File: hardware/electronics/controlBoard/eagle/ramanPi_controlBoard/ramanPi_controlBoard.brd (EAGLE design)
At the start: 149.8 x 98.7 mm, 17 parts

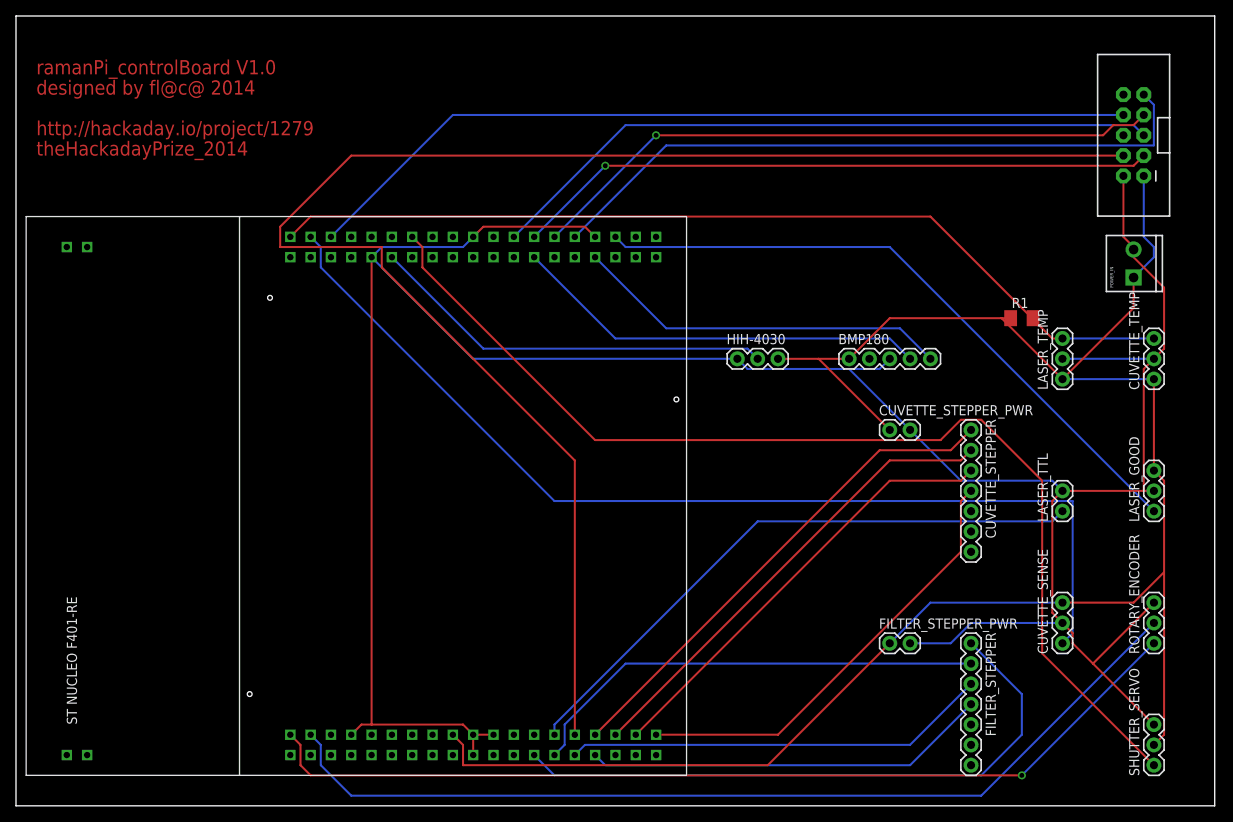
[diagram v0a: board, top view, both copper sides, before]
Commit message: re-routed controlBoard layout
controlBoard board layout redone..
Adjusted stepper controller placement
Adjusted board size
Added svg exports for top and bottom layers
Added top and bottom studio files for cameo
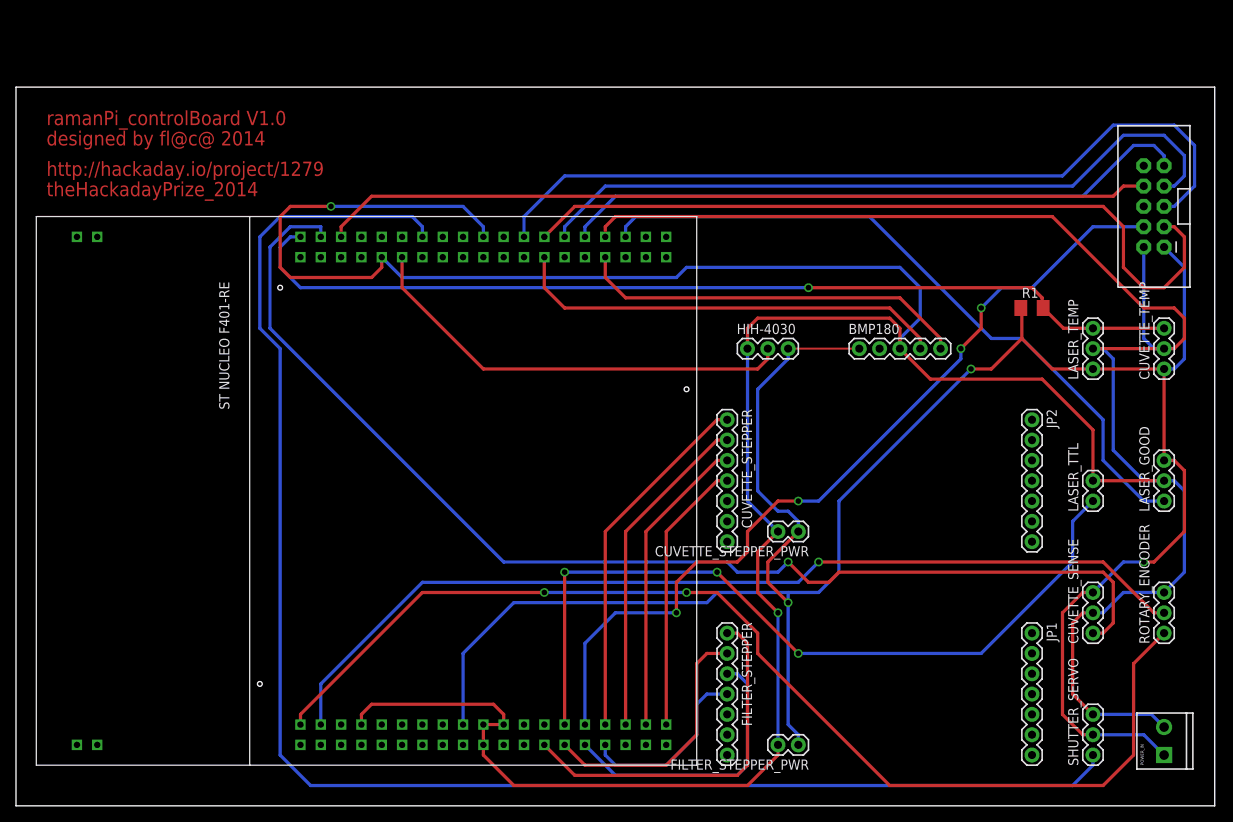
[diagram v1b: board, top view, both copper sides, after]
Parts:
- added JP1, JP2: (no value), SparkFun-Connectors:1X07
- moved POWER_IN 59.8 mm to (143.5, 6.35)
- moved CUVETTE_STEPPER 30.5 mm to (88.9, 48.3)
- moved FILTER_STEPPER 30.5 mm to (88.9, 21.6)
- moved CUVETTE_STEPPER_PWR 17.1 mm to (97.8, 34.3), turned to 180 degrees
- moved FILTER_STEPPER_PWR 17.1 mm to (97.8, 7.62), turned to 180 degrees
- moved POWER_CONTROL_BOARD 9.25 mm to (142.2, 74.9)
- moved SHUTTER_SERVO 7.73 mm to (134.6, 6.35)
- moved LASER_TTL 4.02 mm to (134.6, 38.1)
- moved CUVETTE_SENSE 4.02 mm to (134.6, 21.6)
- moved LASER_TEMP 4.02 mm to (134.6, 54.6)
- moved U$1 1.80 mm to (85.1, 5.08)
- moved BMP180 1.80 mm to (105.4, 57.1)
- moved HIH-4030 1.80 mm to (91.4, 57.1)
- moved R1 1.80 mm to (127.0, 62.2)
- moved LASER_GOOD 1.80 mm to (143.5, 38.1)
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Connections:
- net N$27 renamed GROUND
- net N$3 renamed +5V
- removed net NC6: U$1.NC6
- new net +3V3: U$1.+3V3
- new net U5V: U$1.U5V
- new net VIN: U$1.VIN
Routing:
- net GROUND: track 345.2 -> 501.9 mm, vias 0 -> 2
- net N$7: track 195.3 -> 107.5 mm, vias 0 -> 4
- net N$14: track 136.3 -> 194.5 mm
- net +5V: track 245.5 -> 278.0 mm, vias 0 -> 3
- net N$16: track 78.2 -> 45.8 mm
- net N$19: track 50.7 -> 23.0 mm
- net N$17: track 58.3 -> 32.4 mm
- net N$8: track 75.8 -> 100.2 mm, vias 0 -> 3
- net N$24: track 118.4 -> 141.6 mm, vias 1 -> 2
- net N$23: track 55.7 -> 34.4 mm
- net N$4: track 128.7 -> 147.6 mm, vias 0 -> 1
- net N$21: track 59.2 -> 41.6 mm
- net N$20: track 62.8 -> 45.2 mm
- net N$22: track 55.6 -> 38.0 mm
- net N$18: track 53.2 -> 35.7 mm
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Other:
- board size 149.8 x 98.7 mm -> 149.8 x 89.8 mm

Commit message: finalizing controlBoard layout
finalizing controlBoard layout
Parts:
- added U$2: (no value), SparkFun-Aesthetics:OSHW-LOGO-L
- moved FILTER_STEPPER_PWR 1.27 mm to (97.8, 6.35)
- moved CUVETTE_STEPPER_PWR 1.27 mm to (97.8, 33.0)
- moved JP1 1.27 mm to (125.7, 21.6)
- moved JP2 1.27 mm to (125.7, 48.3)
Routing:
- net N$3: track 0.00 -> 24.1 mm
- net N$31: track 0.00 -> 7.18 mm
- net N$29: track 0.00 -> 3.59 mm
- net N$32: track 0.00 -> 3.59 mm
- net N$30: track 0.00 -> 3.59 mm
- net N$26: track 0.00 -> 2.54 mm
- net N$28: track 0.00 -> 2.54 mm
- net N$27: track 0.00 -> 1.27 mm
- net GROUND: track 501.9 -> 500.8 mm
- net N$8: track 100.2 -> 99.4 mm
- net +5V: track 278.0 -> 277.5 mm
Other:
- board text added: "+"
- board text added: "1"
- board text added: "AFPID:1603"
- board text added: "Gnd"
- board text added: "HIH-4030"
- board text added: "Pos"
- board text added: "PowerIn"
- board text added: "R1"
- board text added: "SFE:SEN-09569"
- board text added: "ST_Nucleo_F401RE"
- board text added: "ULN2003"
- board text added: "bmp180"
- board text added: "cuvSense"
- board text added: "cuvTemp"
- board text added: "cuvetteStepper"
- board text added: "encoder"
- board text added: "filterStepper"
- board text added: "in1"
- board text added: "laserGood"
- board text added: "laserTTL"
- board text added: "laserTemp"
- board text added: "powerControlBoard"
- board text added: "ramanPi"
- board text added: "released under the GNU Public License V2"
- board text added: "shutterSvo"

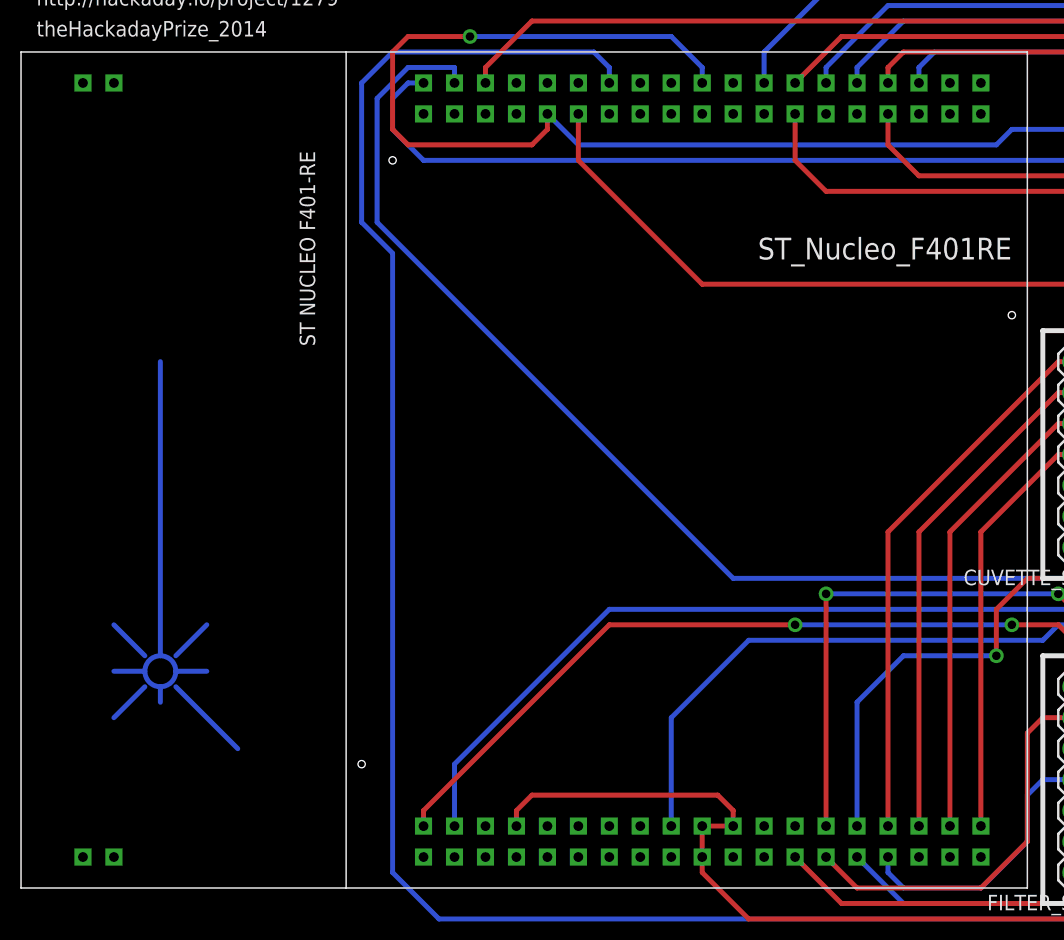
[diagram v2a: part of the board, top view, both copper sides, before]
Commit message: updated Nucleo library in all board layouts
Updated Nucleo F401_RE library for better drill hole sizes
updated all boards to include new library changes
---need to update all studio files, svg, etc..
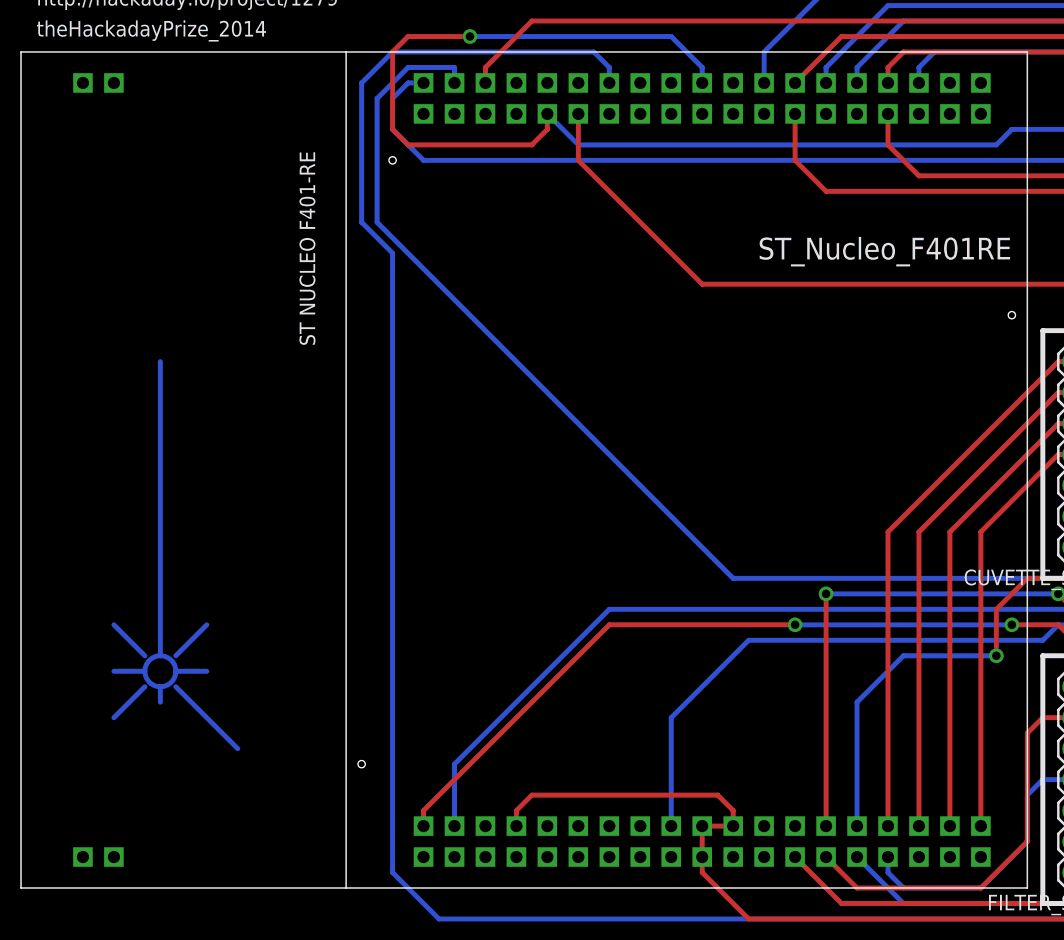
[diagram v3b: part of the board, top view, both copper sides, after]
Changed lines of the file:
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@@
 </signal>
 </signals>
+<errors>
+</errors>
 </board>
 </drawing>

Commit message: update
updated all boards and schematics
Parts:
- added FID1, FID2: FIDUCIAL1X2, SparkFun-Aesthetics:FIDUCIAL-1X2
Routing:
- net GROUND: track 500.8 -> 509.8 mm
- net N$4: track 147.6 -> 151.8 mm, vias 1 -> 3
- net N$45: track 0.00 -> 2.54 mm
- net N$41: track 0.00 -> 2.54 mm
- net N$37: track 0.00 -> 2.54 mm
- net N$35: track 0.00 -> 2.54 mm
- net N$47: track 0.00 -> 2.54 mm
- net N$44: track 0.00 -> 2.54 mm
- net N$42: track 0.00 -> 2.54 mm
- net N$39: track 0.00 -> 2.54 mm
- net N$36: track 0.00 -> 2.54 mm
- net N$34: track 0.00 -> 2.54 mm
- net N$43: track 0.00 -> 2.54 mm
- net N$33: track 0.00 -> 2.54 mm
- net N$48: track 0.00 -> 2.54 mm
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
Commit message: added reset circuitry to all stm32 boards
added reset circuitry for raspi to reset each board from remote.
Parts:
- added Q1: 2n2222, semicon-smd-ipc:SOT23
- added R2: 10k, adafruit:M1206
- added RASPI_RESET: M02PTH, SparkFun-Connectors:1X02
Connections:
- new net N$49: Q1.3, R2.1, U$1.NRST
- new net N$50: Q1.1, RASPI_RESET.1
- net +5V: now also R2.2
- net GROUND: now also Q1.2, RASPI_RESET.2
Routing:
- net N$50: track 0.00 -> 101.5 mm, vias 0 -> 2
- net GROUND: track 509.8 -> 525.4 mm
- net N$49: track 0.00 -> 15.3 mm, vias 0 -> 1
- net +5V: track 276.2 -> 280.6 mm, vias 3 -> 4
- net N$25: track 119.4 -> 122.4 mm
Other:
- board text added: "Q1"
- board text added: "R2"
- board text added: "raspiReset"
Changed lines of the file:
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@@
 <layer number="19" name="Unrouted" color="6" fill="1" visible="yes" active="yes"/>
 <layer number="20" name="Dimension" color="15" fill="1" visible="yes" active="yes"/>
-<layer number="21" name="tPlace" color="7" fill="1" visible="yes" active="yes"/>
-<layer number="22" name="bPlace" color="7" fill="1" visible="yes" active="yes"/>
-<layer number="23" name="tOrigins" color="15" fill="1" visible="yes" active="yes"/>
-<layer number="24" name="bOrigins" color="15" fill="1" visible="yes" active="yes"/>
+<layer number="21" name="tPlace" color="7" fill="1" visible="no" active="yes"/>
+<layer number="22" name="bPlace" color="7" fill="1" visible="no" active="yes"/>
+<layer number="23" name="tOrigins" color="15" fill="1" visible="no" active="yes"/>
+<layer number="24" name="bOrigins" color="15" fill="1" visible="no" active="yes"/>
 <layer number="25" name="tNames" color="7" fill="1" visible="no" active="yes"/>
 <layer number="26" name="bNames" color="7" fill="1" visible="no" active="yes"/>
@@
 <text x="91.44" y="59.69" size="1.016" layer="21" font="vector" rot="R90">SFE:SEN-09569</text>
 <text x="3.81" y="80.01" size="1.27" layer="21" font="vector">released under the GNU Public License V2</text>
+<text x="52.07" y="76.2" size="1.778" layer="21">raspiReset</text>
+<text x="45.72" y="21.59" size="1.778" layer="21">Q1</text>
+<text x="58.42" y="21.59" size="1.778" layer="21">R2</text>
 </plain>
 <attributes>
@@
 <element name="FID1" library="SparkFun-Aesthetics" package="FIDUCIAL-1X2" value="FIDUCIAL1X2" x="2.54" y="2.54"/>
 <element name="FID2" library="SparkFun-Aesthetics" package="FIDUCIAL-1X2" value="FIDUCIAL1X2" x="144.78" y="87.63"/>
+<element name="Q1" library="semicon-smd-ipc" package="SOT23" value="2n2222" x="50.8" y="20.32" rot="R270"/>
+<element name="R2" library="adafruit" package="M1206" value="10k" x="54.61" y="24.13"/>
+<element name="RASPI_RESET" library="SparkFun-Connectors" package="1X02" value="M02PTH" x="55.88" y="80.01"/>
 </elements>
 <signals>
@@
 <wire x1="102.87" y1="29.21" x2="100.33" y2="26.67" width="0.4064" layer="16"/>
 <wire x1="86.36" y1="25.4" x2="62.23" y2="25.4" width="0.4064" layer="16"/>
-<wire x1="62.23" y1="25.4" x2="55.88" y2="19.05" width="0.4064" layer="16"/>
+<wire x1="62.23" y1="25.4" x2="57.15" y2="20.32" width="0.4064" layer="16"/>
+<wire x1="57.15" y1="20.32" x2="55.88" y2="19.05" width="0.4064" layer="16"/>
 <wire x1="55.88" y1="19.05" x2="55.88" y2="10.16" width="0.4064" layer="16"/>
 <wire x1="143.51" y1="69.85" x2="146.05" y2="67.31" width="0.4064" layer="16"/>
@@
 <wire x1="87.63" y1="26.67" x2="86.36" y2="25.4" width="0.4064" layer="16"/>
 <wire x1="100.33" y1="26.67" x2="96.52" y2="26.67" width="0.4064" layer="16"/>
+<contactref element="R2" pad="2"/>
+<wire x1="56.01" y1="24.13" x2="56.01" y2="21.72" width="0.4064" layer="1"/>
+<wire x1="56.01" y1="21.72" x2="55.88" y2="21.59" width="0.4064" layer="1"/>
+<via x="55.88" y="21.59" extent="1-16" drill="0.7"/>
+<wire x1="57.15" y1="20.32" x2="55.88" y2="21.59" width="0.4064" layer="16"/>
 </signal>
 <signal name="N$5">
@@
 <via x="100.33" y="30.48" extent="1-16" drill="0.7"/>
 <wire x1="100.33" y1="30.48" x2="97.79" y2="27.94" width="0.4064" layer="16"/>
-<wire x1="50.8" y1="27.94" x2="38.1" y2="15.24" width="0.4064" layer="16"/>
-<wire x1="38.1" y1="15.24" x2="38.1" y2="10.16" width="0.4064" layer="16"/>
+<wire x1="45.72" y1="27.94" x2="38.1" y2="20.32" width="0.4064" layer="16"/>
+<wire x1="38.1" y1="20.32" x2="38.1" y2="10.16" width="0.4064" layer="16"/>
 <wire x1="143.51" y1="24.13" x2="142.24" y2="24.13" width="0.4064" layer="1"/>
 <wire x1="142.24" y1="24.13" x2="135.89" y2="30.48" width="0.4064" layer="1"/>
 <wire x1="135.89" y1="30.48" x2="100.33" y2="30.48" width="0.4064" layer="1"/>
-<wire x1="97.79" y1="27.94" x2="50.8" y2="27.94" width="0.4064" layer="16"/>
+<wire x1="97.79" y1="27.94" x2="45.72" y2="27.94" width="0.4064" layer="16"/>
 </signal>
 <signal name="N$4">
@@
 <wire x1="43.18" y1="10.16" x2="43.18" y2="11.43" width="0.4064" layer="1"/>
 <wire x1="43.18" y1="11.43" x2="44.45" y2="12.7" width="0.4064" layer="1"/>
-<wire x1="44.45" y1="12.7" x2="59.69" y2="12.7" width="0.4064" layer="1"/>
+<wire x1="49.7" y1="12.7" x2="59.69" y2="12.7" width="0.4064" layer="1"/>
 <wire x1="59.69" y1="12.7" x2="60.96" y2="11.43" width="0.4064" layer="1"/>
 <wire x1="60.96" y1="11.43" x2="60.96" y2="10.16" width="0.4064" layer="1"/>
@@
 <wire x1="46.99" y1="66.04" x2="45.72" y2="67.31" width="0.4064" layer="16"/>
 <wire x1="45.72" y1="67.31" x2="45.72" y2="68.58" width="0.4064" layer="16"/>
+<contactref element="Q1" pad="2"/>
+<contactref element="RASPI_RESET" pad="2"/>
+<wire x1="44.45" y1="12.7" x2="49.7" y2="12.7" width="0.4064" layer="1"/>
+<wire x1="49.7" y1="12.7" x2="49.7" y2="19.37" width="0.4064" layer="1"/>
+<wire x1="58.42" y1="80.01" x2="58.42" y2="71.12" width="0.4064" layer="16"/>
 </signal>
 <signal name="U5V">
@@
 <wire x1="142.24" y1="16.51" x2="144.78" y2="16.51" width="0.4064" layer="1"/>
 </signal>
+<signal name="N$49">
+<contactref element="U$1" pad="NRST"/>
+<contactref element="Q1" pad="3"/>
+<contactref element="R2" pad="1"/>
+<wire x1="51.9" y1="20.32" x2="51.9" y2="22.69" width="0.4064" layer="1"/>
+<wire x1="51.9" y1="22.69" x2="53.34" y2="24.13" width="0.4064" layer="1"/>
+<wire x1="53.34" y1="24.13" x2="53.21" y2="24.13" width="0.4064" layer="1"/>
+<wire x1="50.8" y1="10.16" x2="50.8" y2="15.24" width="0.4064" layer="16"/>
+<wire x1="50.8" y1="15.24" x2="52.07" y2="16.51" width="0.4064" layer="16"/>
+<via x="52.07" y="16.51" extent="1-16" drill="0.7"/>
+<wire x1="52.07" y1="16.51" x2="52.07" y2="20.15" width="0.4064" layer="1"/>
+<wire x1="52.07" y1="20.15" x2="51.9" y2="20.32" width="0.4064" layer="1"/>
+</signal>
+<signal name="N$50">
+<contactref element="Q1" pad="1"/>
+<contactref element="RASPI_RESET" pad="1"/>
+<wire x1="49.7" y1="21.27" x2="47.94" y2="21.27" width="0.4064" layer="1"/>
+<wire x1="47.94" y1="21.27" x2="45.72" y2="19.05" width="0.4064" layer="1"/>
+<wire x1="45.72" y1="19.05" x2="45.72" y2="17.78" width="0.4064" layer="1"/>
+<via x="45.72" y="17.78" extent="1-16" drill="0.7"/>
+<wire x1="45.72" y1="17.78" x2="41.91" y2="17.78" width="0.4064" layer="16"/>
+<wire x1="41.91" y1="17.78" x2="40.64" y2="19.05" width="0.4064" layer="16"/>
+<via x="40.64" y="19.05" extent="1-16" drill="0.7"/>
+<wire x1="40.64" y1="19.05" x2="40.64" y2="52.07" width="0.4064" layer="1"/>
+<wire x1="40.64" y1="52.07" x2="27.94" y2="64.77" width="0.4064" layer="1"/>
+<wire x1="27.94" y1="64.77" x2="27.94" y2="72.39" width="0.4064" layer="1"/>
+<wire x1="27.94" y1="72.39" x2="35.56" y2="80.01" width="0.4064" layer="1"/>
+<wire x1="35.56" y1="80.01" x2="55.88" y2="80.01" width="0.4064" layer="1"/>
+</signal>
 </signals>
